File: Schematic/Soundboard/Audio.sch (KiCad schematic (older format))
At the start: 8 parts, among them J4 AudioJack3, U5 CS4334, U6 LM4811

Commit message: Complete part selection. Start connections
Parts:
- J1: renamed from J4; footprint Connector_Audio:Jack_3.5mm_CUI_SJ-3523-SMT_Horizontal -> Connector_Audio:Jack_3.5mm_CUI_SJ1-3533NG_Horizontal
- U3: renamed from U5; footprint Package_SO:SOIC-8-N7_3.9x4.9mm_P1.27mm -> Package_SO:SOIC-8_3.9x4.9mm_P1.27mm
- renumbered C5 to C1, C6 to C2, C7 to C3, C8 to C4, C9 to C5, U6 to U2
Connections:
- net labels added: AMP_CLOCK, AMP_SHUTDOWN, AMP_UD, DAC_LRCLK, DAC_MCLK, DAC_SCLK, DAC_SDATA, V_PERIPH_5V
- net labels removed: +5V
- wire segments 15 -> 19
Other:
- moved on the sheet: C1, C2, C3, C4, C5, J1, U2, U3

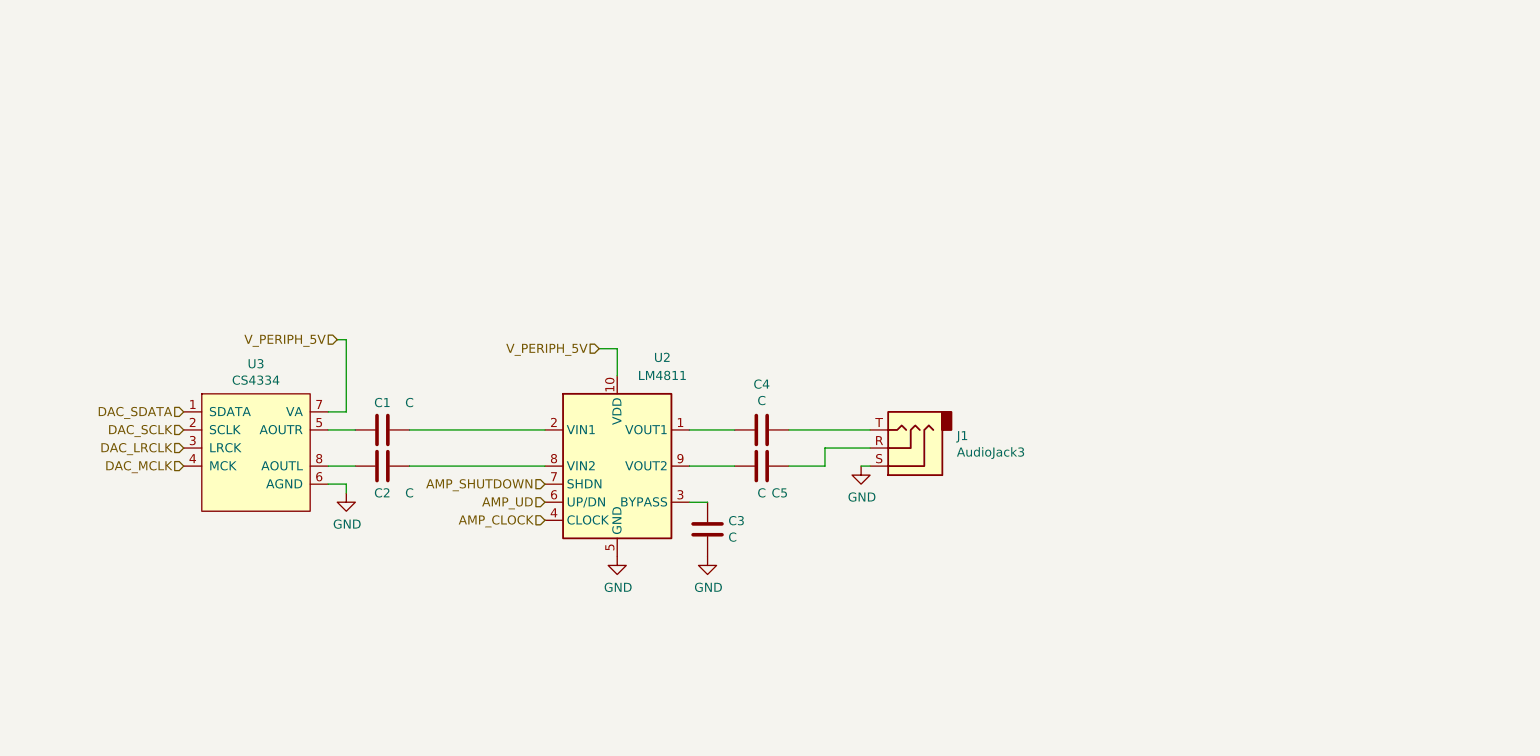
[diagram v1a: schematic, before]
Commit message: Complete connections except for display to be chosen
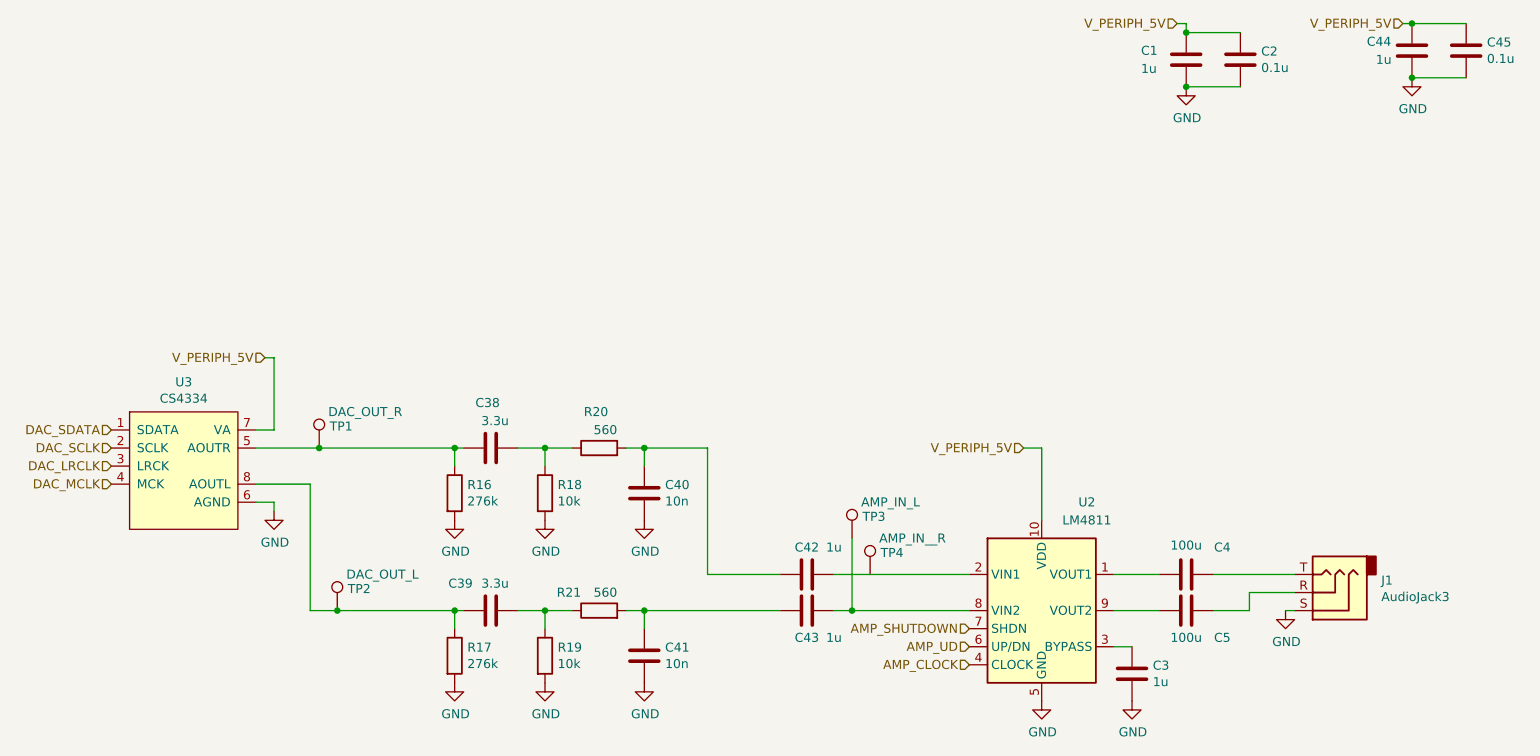
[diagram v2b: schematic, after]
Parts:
- added C1: 1u, symbol Device:C
- added C2, C45: 0.1u, symbol Device:C
- added C38, C39: 3.3u, symbol Device:C
- added C40, C41: 10n, symbol Device:C
- added C44: 1u, Capacitor_SMD:C_0603_1608Metric_Pad1.05x0.95mm_HandSolder, symbol Device:C
- added R16, R17: 276k, symbol Device:R
- added R18, R19: 10k, symbol Device:R
- added R20, R21: 560, symbol Device:R
- added TP1: DAC_OUT_R, symbol Connector:TestPoint
- added TP2: DAC_OUT_L, symbol Connector:TestPoint
- added TP3: AMP_IN_L, symbol Connector:TestPoint
- added TP4: AMP_IN__R, symbol Connector:TestPoint
- C3: value C -> 1u
- C4, C5: value C -> 100u
- C42: renamed from C1; value C -> 1u
- C43: renamed from C2; value C -> 1u
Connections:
- net GND: now also C1.2, C2.2, C40.2, C41.2, C44.2, C45.2, R16.2, R17.2, R18.2, R19.2
- net V_PERIPH_5V: now also C1.1, C2.1, C44.1, C45.1
- net at C43.1, U2.8 (VIN2): now also TP3.1
- net at C42.2: now also C40.1, R20.2; no longer U3.5 (AOUTR)
- net at C43.2: now also C41.1, R21.2; no longer U3.8 (AOUTL)
- new net: C38.1, R16.1, TP1.1, U3.5 (AOUTR)
- new net: C39.1, R17.1, TP2.1, U3.8 (AOUTL)
- new net: C39.2, R19.1, R21.1
- new net: C38.2, R18.1, R20.1
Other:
- moved on the sheet: C3, C4, C42, C43, C5, J1, U2, U3

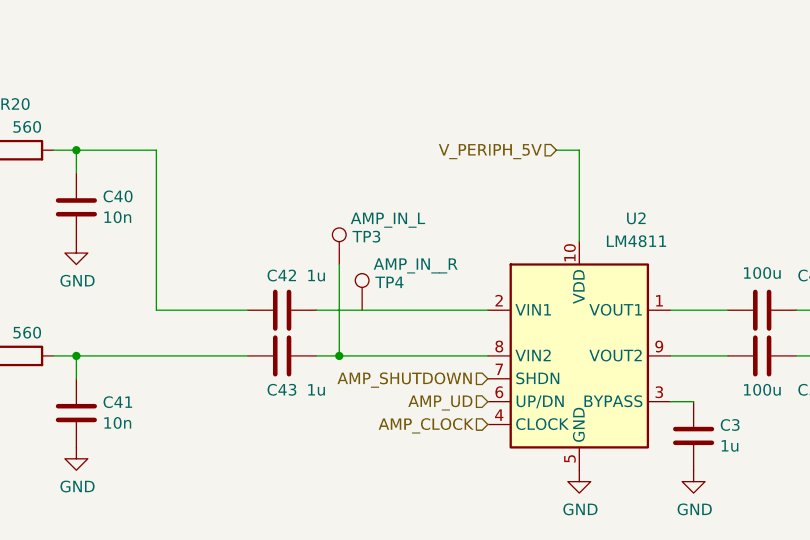
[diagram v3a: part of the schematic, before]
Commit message: Choose display. Complete schematic
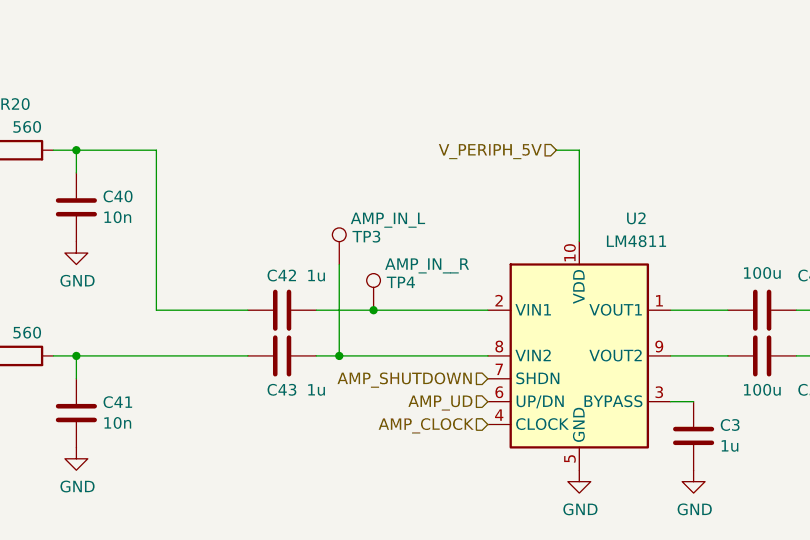
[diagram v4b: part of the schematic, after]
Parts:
- C1, C2, C38, C39, C40, C41, C45: footprint (none) -> Capacitor_SMD:C_0603_1608Metric_Pad1.05x0.95mm_HandSolder
- R16, R17, R18, R19, R20, R21: footprint (none) -> Resistor_SMD:R_0603_1608Metric_Pad1.05x0.95mm_HandSolder
- TP1, TP2, TP3, TP4: footprint (none) -> TestPoint:TestPoint_Pad_D2.0mm
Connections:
- net at C42.1, U2.2 (VIN1): now also TP4.1
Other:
- moved on the sheet: TP4
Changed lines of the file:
@@
 	7000 4200 7100 4200
 Wire Wire Line
-	7000 4000 7750 4000
+	7000 4000 7250 4000
 Wire Wire Line
 	9100 4200 9300 4200
@@
 F 0 "C2" H 9365 1196 50  0000 L CNN
 F 1 "0.1u" H 9365 1105 50  0000 L CNN
-F 2 "" H 9288 1000 50  0001 C CNN
+F 2 "Capacitor_SMD:C_0603_1608Metric_Pad1.05x0.95mm_HandSolder" H 9288 1000 50  0001 C CNN
 F 3 "~" H 9250 1150 50  0001 C CNN
 	1    9250 1150
@@
 F 0 "C1" H 8700 1200 50  0000 L CNN
 F 1 "1u" H 8700 1100 50  0000 L CNN
-F 2 "" H 8988 1000 50  0001 C CNN
+F 2 "Capacitor_SMD:C_0603_1608Metric_Pad1.05x0.95mm_HandSolder" H 8988 1000 50  0001 C CNN
 F 3 "~" H 8950 1150 50  0001 C CNN
 	1    8950 1150
@@
 F 0 "C41" H 6065 4496 50  0000 L CNN
 F 1 "10n" H 6065 4405 50  0000 L CNN
-F 2 "" H 5988 4300 50  0001 C CNN
+F 2 "Capacitor_SMD:C_0603_1608Metric_Pad1.05x0.95mm_HandSolder" H 5988 4300 50  0001 C CNN
 F 3 "~" H 5950 4450 50  0001 C CNN
 	1    5950 4450
@@
 F 0 "C39" V 5250 4300 50  0000 L CNN
 F 1 "3.3u" V 5250 4100 50  0000 L CNN
-F 2 "" H 5138 4050 50  0001 C CNN
+F 2 "Capacitor_SMD:C_0603_1608Metric_Pad1.05x0.95mm_HandSolder" H 5138 4050 50  0001 C CNN
 F 3 "~" H 5100 4200 50  0001 C CNN
 	1    5100 4200
@@
 F 0 "R21" V 5800 4300 50  0000 L CNN
 F 1 "560" V 5800 4100 50  0000 L CNN
-F 2 "" V 5630 4200 50  0001 C CNN
+F 2 "Resistor_SMD:R_0603_1608Metric_Pad1.05x0.95mm_HandSolder" V 5630 4200 50  0001 C CNN
 F 3 "~" H 5700 4200 50  0001 C CNN
 	1    5700 4200
@@
 F 0 "R17" H 4970 4496 50  0000 L CNN
 F 1 "276k" H 4970 4405 50  0000 L CNN
-F 2 "" V 4830 4450 50  0001 C CNN
+F 2 "Resistor_SMD:R_0603_1608Metric_Pad1.05x0.95mm_HandSolder" V 4830 4450 50  0001 C CNN
 F 3 "~" H 4900 4450 50  0001 C CNN
 	1    4900 4450
@@
 F 0 "R19" H 5470 4496 50  0000 L CNN
 F 1 "10k" H 5470 4405 50  0000 L CNN
-F 2 "" V 5330 4450 50  0001 C CNN
+F 2 "Resistor_SMD:R_0603_1608Metric_Pad1.05x0.95mm_HandSolder" V 5330 4450 50  0001 C CNN
 F 3 "~" H 5400 4450 50  0001 C CNN
 	1    5400 4450
@@
 F 0 "C40" H 6065 3596 50  0000 L CNN
 F 1 "10n" H 6065 3505 50  0000 L CNN
-F 2 "" H 5988 3400 50  0001 C CNN
+F 2 "Capacitor_SMD:C_0603_1608Metric_Pad1.05x0.95mm_HandSolder" H 5988 3400 50  0001 C CNN
 F 3 "~" H 5950 3550 50  0001 C CNN
 	1    5950 3550
@@
 F 0 "C38" V 5350 3250 50  0000 L CNN
 F 1 "3.3u" V 5250 3200 50  0000 L CNN
-F 2 "" H 5138 3150 50  0001 C CNN
+F 2 "Capacitor_SMD:C_0603_1608Metric_Pad1.05x0.95mm_HandSolder" H 5138 3150 50  0001 C CNN
 F 3 "~" H 5100 3300 50  0001 C CNN
 	1    5100 3300
@@
 F 0 "R20" V 5900 3250 50  0000 L CNN
 F 1 "560" V 5800 3200 50  0000 L CNN
-F 2 "" V 5630 3300 50  0001 C CNN
+F 2 "Resistor_SMD:R_0603_1608Metric_Pad1.05x0.95mm_HandSolder" V 5630 3300 50  0001 C CNN
 F 3 "~" H 5700 3300 50  0001 C CNN
 	1    5700 3300
@@
 F 0 "R16" H 4970 3596 50  0000 L CNN
 F 1 "276k" H 4970 3505 50  0000 L CNN
-F 2 "" V 4830 3550 50  0001 C CNN
+F 2 "Resistor_SMD:R_0603_1608Metric_Pad1.05x0.95mm_HandSolder" V 4830 3550 50  0001 C CNN
 F 3 "~" H 4900 3550 50  0001 C CNN
 	1    4900 3550
@@
 F 0 "R18" H 5470 3596 50  0000 L CNN
 F 1 "10k" H 5470 3505 50  0000 L CNN
-F 2 "" V 5330 3550 50  0001 C CNN
+F 2 "Resistor_SMD:R_0603_1608Metric_Pad1.05x0.95mm_HandSolder" V 5330 3550 50  0001 C CNN
 F 3 "~" H 5400 3550 50  0001 C CNN
 	1    5400 3550
@@
 F 0 "C45" H 10615 1146 50  0000 L CNN
 F 1 "0.1u" H 10615 1055 50  0000 L CNN
-F 2 "" H 10538 950 50  0001 C CNN
+F 2 "Capacitor_SMD:C_0603_1608Metric_Pad1.05x0.95mm_HandSolder" H 10538 950 50  0001 C CNN
 F 3 "~" H 10500 1100 50  0001 C CNN
 	1    10500 1100
@@
 F 0 "TP1" H 4208 3420 50  0000 L CNN
 F 1 "DAC_OUT_R" H 4200 3500 50  0000 L CNN
-F 2 "" H 4350 3300 50  0001 C CNN
+F 2 "TestPoint:TestPoint_Pad_D2.0mm" H 4350 3300 50  0001 C CNN
 F 3 "~" H 4350 3300 50  0001 C CNN
 	1    4150 3300
@@
 F 0 "TP2" H 4308 4320 50  0000 L CNN
 F 1 "DAC_OUT_L" H 4300 4400 50  0000 L CNN
-F 2 "" H 4450 4200 50  0001 C CNN
+F 2 "TestPoint:TestPoint_Pad_D2.0mm" H 4450 4200 50  0001 C CNN
 F 3 "~" H 4450 4200 50  0001 C CNN
 	1    4250 4200
@@
 L Connector:TestPoint TP4
 U 1 1 5F71642F
-P 7200 4000
-F 0 "TP4" H 7258 4120 50  0000 L CNN
-F 1 "AMP_IN__R" H 7250 4200 50  0000 L CNN
-F 2 "" H 7400 4000 50  0001 C CNN
-F 3 "~" H 7400 4000 50  0001 C CNN
-	1    7200 4000
+P 7250 4000
+F 0 "TP4" H 7308 4120 50  0000 L CNN
+F 1 "AMP_IN__R" H 7300 4200 50  0000 L CNN
+F 2 "TestPoint:TestPoint_Pad_D2.0mm" H 7450 4000 50  0001 C CNN
+F 3 "~" H 7450 4000 50  0001 C CNN
+	1    7250 4000
 	1    0    0    -1
 $EndComp
@@
 F 0 "TP3" H 7158 3920 50  0000 L CNN
 F 1 "AMP_IN_L" H 7150 4000 50  0000 L CNN
-F 2 "" H 7300 3800 50  0001 C CNN
+F 2 "TestPoint:TestPoint_Pad_D2.0mm" H 7300 3800 50  0001 C CNN
 F 3 "~" H 7300 3800 50  0001 C CNN
 	1    7100 3800
@@
 Wire Wire Line
 	8150 3300 8150 3700
+Connection ~ 7250 4000
+Wire Wire Line
+	7250 4000 7750 4000
 $EndSCHEMATC
